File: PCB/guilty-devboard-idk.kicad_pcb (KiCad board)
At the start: 6 copper layers, 17.8 x 33.1 mm, 60 parts, among them J1 USB_C_Receptacle_USB2.0_16P, Q1 SP2038CNQ, U1 nRF54LM20A-QGAA, U2 SGM40567-4.2XG/TR, U3 Xiao nRF52840 Connectors, U4 TCA9536, U5 FH9261-G3JH, U6 BD83070GWL-E2, Y1 32MHz, Y2 32.768kHz

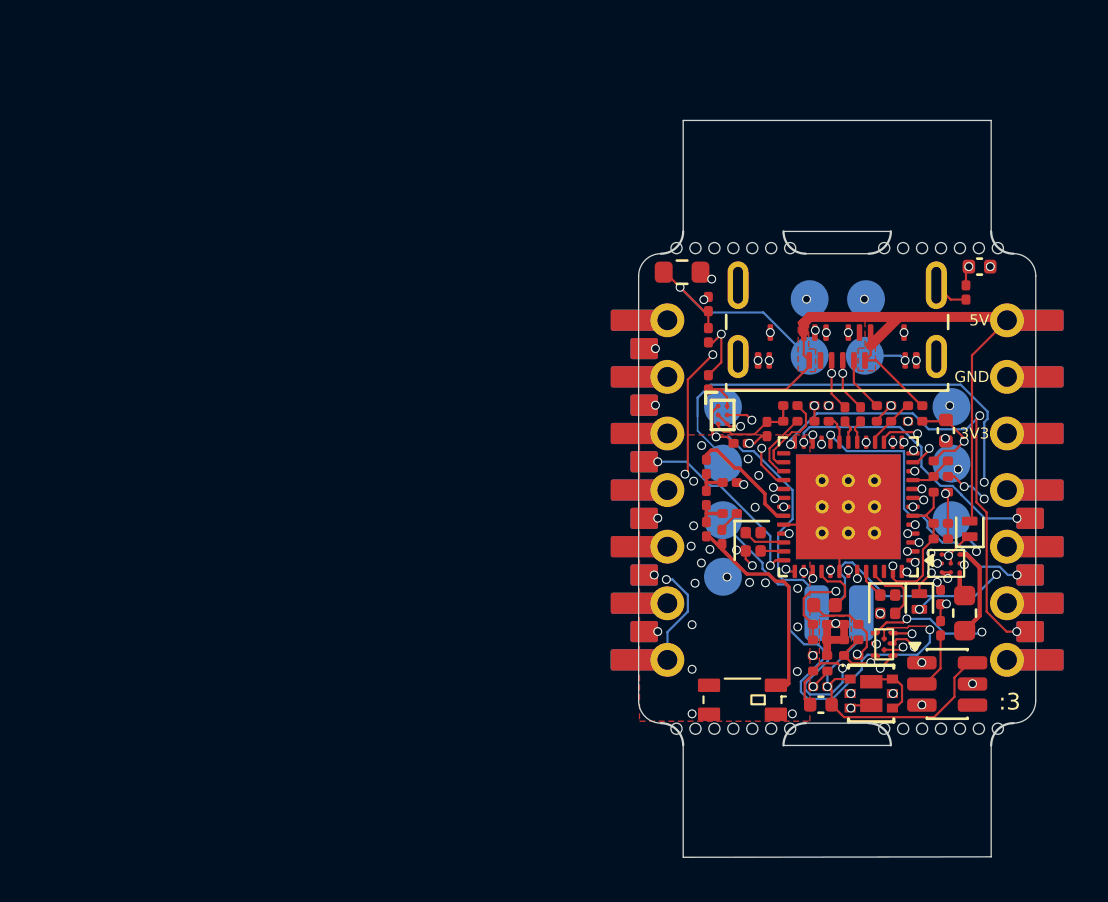
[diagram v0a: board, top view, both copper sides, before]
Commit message: fix pads being slightly off, should now match xiao pretty much perfectly
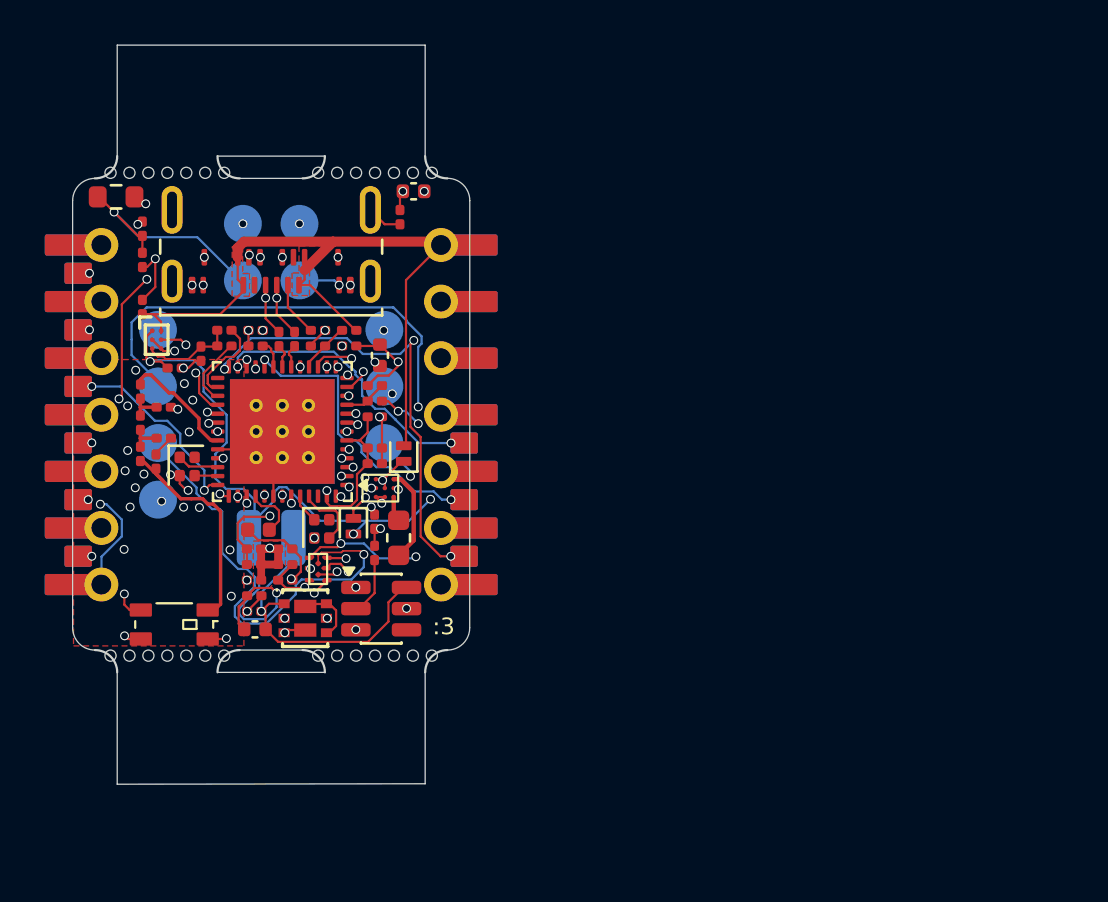
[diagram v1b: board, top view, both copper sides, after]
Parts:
- U3: value Xiao nRF52840 Connectors -> ~
- moved AE1 25.7 mm to (54.1, 63.7)
- moved C1 25.6 mm to (63.3, 51.6)
- moved C12 25.6 mm to (57.7, 63.1)
- moved C14 25.6 mm to (52.6, 49.5)
- moved C16 25.6 mm to (57.7, 63.9)
- moved C21 25.6 mm to (52.6, 47.3)
- moved C3 25.6 mm to (53.2, 56.4)
- moved C4 25.6 mm to (59.0, 61.7)
- moved C6 25.6 mm to (59.0, 61.0)
- moved D6 25.6 mm to (62.1, 59.3)
- moved FB1 25.6 mm to (59.0, 60.3)
- moved L1 25.6 mm to (52.5, 56.0)
- moved L3 25.6 mm to (64.1, 59.8)
- moved L4 25.6 mm to (52.5, 54.6)
- moved L5 25.6 mm to (52.5, 53.2)
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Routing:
- net GND: track 26.5 -> 29.6 mm, vias 41 -> 40
- net +BATT: track 40.0 -> 41.5 mm
- net /IO_EXT_P2_D23: track 8.04 -> 8.91 mm
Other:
- board size 17.8 x 33.1 mm -> 17.8 x 33.2 mm
